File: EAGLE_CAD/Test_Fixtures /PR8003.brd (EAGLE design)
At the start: 116 x 100 mm, 43 parts, among them J1 M3_SCREW_POST

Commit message: Bumped to PR8003
New layout
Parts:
- moved JP2 53.0 mm to (78.0, 76.0), turned to 180 degrees
- moved U$24 51.6 mm to (6.00, 59.0)
- moved VOL 48.4 mm to (89.6, 5.12), turned to 180 degrees
- moved U$23 45.4 mm to (6.00, 11.0)
- moved U$20 42.2 mm to (6.00, 27.0)
- moved R2 39.5 mm to (33.0, 79.0), turned to 270 degrees
- moved U$22 37.2 mm to (6.00, 43.0)
- moved U$1 30.2 mm to (58.1, 28.4)
- moved CN1 27.9 mm to (77.0, 85.0)
- moved R16 22.6 mm to (56.9, 45.8)
- moved R13 21.7 mm to (30.8, 79.0), turned to 270 degrees
- moved R3 21.5 mm to (27.8, 79.0), turned to 270 degrees
- moved R1 21.4 mm to (25.5, 79.0), turned to 270 degrees
- moved JP1 18.9 mm to (33.0, 85.0)
- moved ISP1 16.9 mm to (65.0, 85.0), turned to 270 degrees
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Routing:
- net +5V: track 8.02 -> 188.4 mm, vias 0 -> 5
- net DEV_PRES: track 0.00 -> 138.0 mm, vias 0 -> 1
- net SPK_OUT+: track 0.00 -> 108.9 mm, vias 0 -> 1
- net SPK_OUT-: track 0.00 -> 103.7 mm, vias 0 -> 1
- net TAC2: track 0.00 -> 85.4 mm, vias 0 -> 1
- net TAC3: track 0.00 -> 81.5 mm, vias 0 -> 2
- net TAC1: track 0.00 -> 69.8 mm, vias 0 -> 1
- net ANT: track 0.00 -> 68.3 mm, vias 0 -> 1
- net N$2: track 0.00 -> 68.2 mm
- net N$3: track 0.00 -> 68.0 mm
- net N$4: track 0.00 -> 67.9 mm
- net 3.3V: track 4.76 -> 64.6 mm, vias 0 -> 2
- net COMPARATOR: track 0.00 -> 53.1 mm, vias 0 -> 2
- net A_OUT: track 0.00 -> 52.0 mm
- net REG_ENABLE: track 6.30 -> 56.6 mm
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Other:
- board size 116 x 100 mm -> 100 x 91 mm
- board text added: "PR8003"
- board text added: "SPK"
- board text removed: "1"
- board text removed: "2"
- board text removed: "ETest PR8002"
- board text removed: "EXT SPK"

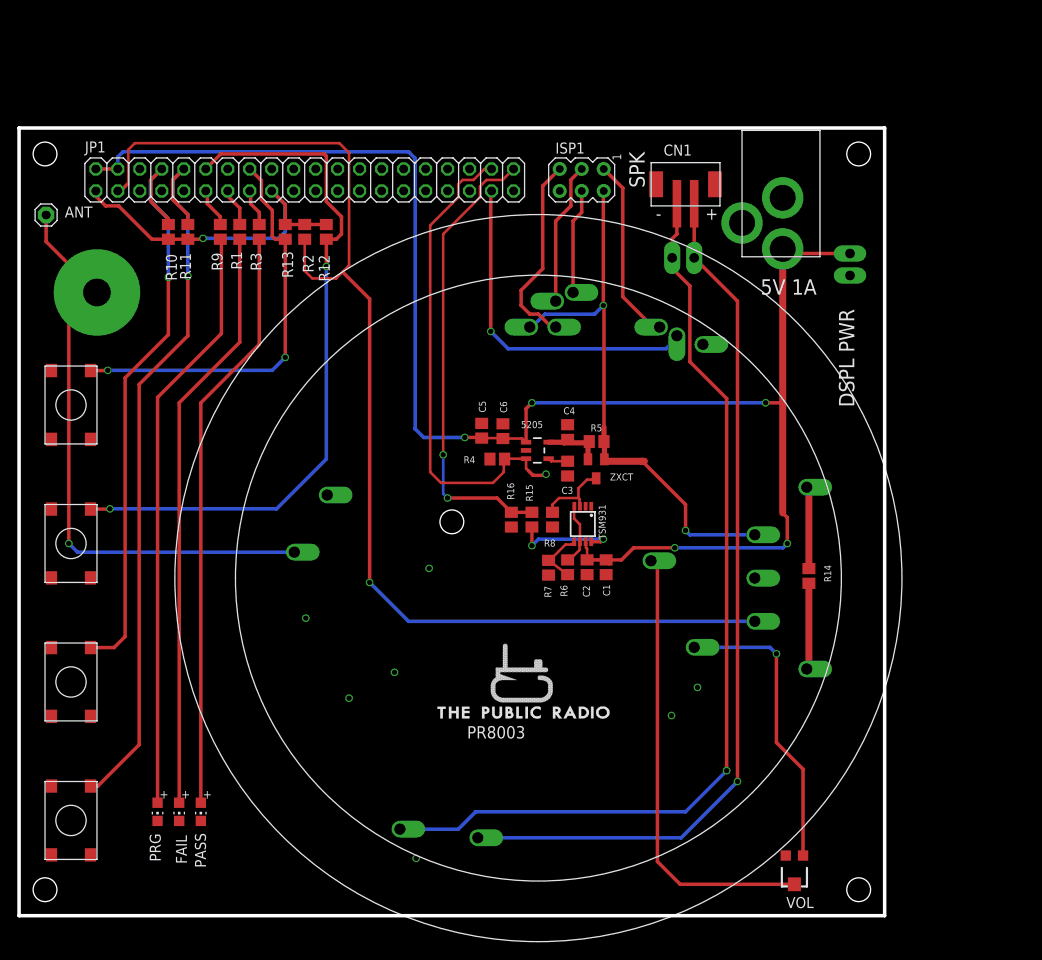
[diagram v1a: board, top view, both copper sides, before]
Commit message: PR8003 Updates
Small layout changes
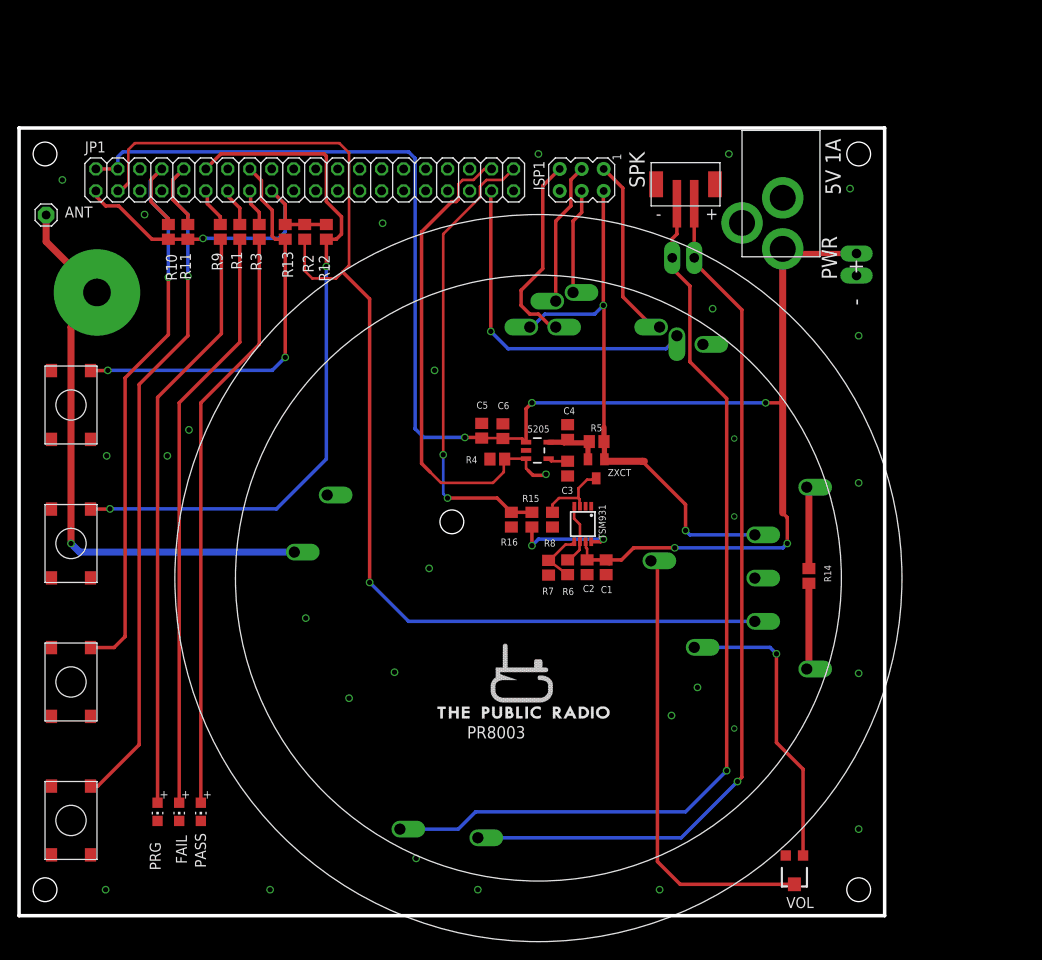
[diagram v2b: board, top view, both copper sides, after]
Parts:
- moved JP3 0.75 mm to (96.8, 76.5)
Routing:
- net REG_ENABLE: track 56.6 -> 57.7 mm
- net +5V: track 188.4 -> 189.1 mm
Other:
- board text added: "- +"
- board text added: "PWR"
- board text removed: "DSPL PWR"

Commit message: PR8003 Updates
Mostly aesthetics. Small routing changes.
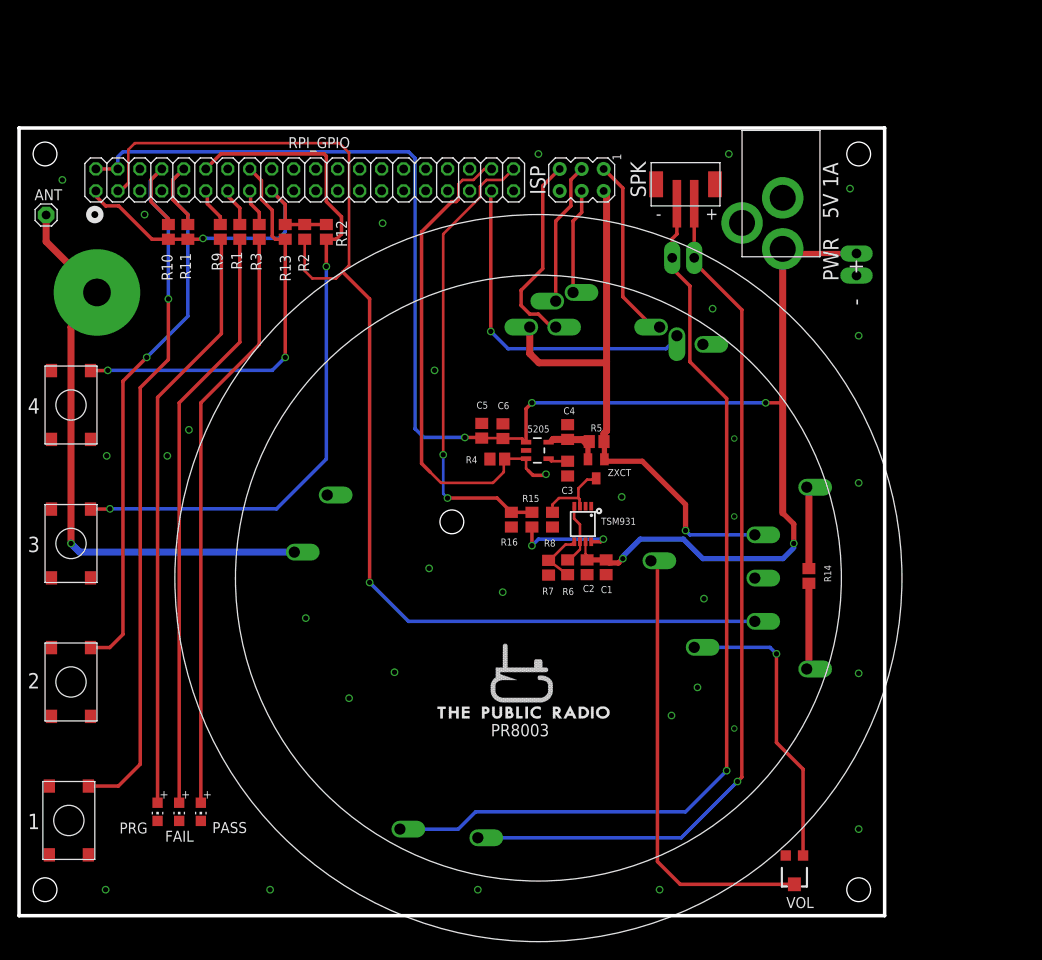
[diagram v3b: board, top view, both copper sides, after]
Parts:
- moved U$20 16.0 mm to (5.75, 11.0)
- moved U$23 16.0 mm to (6.00, 27.0)
- renumbered ISP1 to ISP, JP1 to RPI_GPIO
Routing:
- net TAC1: track 69.8 -> 86.4 mm
- net TAC2: track 85.4 -> 70.2 mm
- net 3.3V: track 64.6 -> 67.6 mm, vias 2 -> 1
- net +5V: track 189.1 -> 190.1 mm
- net N$14: track 7.89 -> 6.96 mm
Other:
- board text added: "1"
- board text added: "2"
- board text added: "3"
- board text added: "4"

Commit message: PR8003 Updates
small changes
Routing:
- net COMPARATOR: track 53.1 -> 56.1 mm
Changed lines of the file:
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@@
 <contactref element="5205" pad="4"/>
 <contactref element="C3" pad="1"/>
-<wire x1="61.4751" y1="52.85" x2="61.1751" y2="52.8" width="0.3048" layer="1"/>
-<wire x1="63.375" y1="52.5" x2="61.4751" y2="52.5" width="0.3048" layer="1"/>
+<wire x1="61.4751" y1="52.85" x2="61.1751" y2="52.8" width="0.4064" layer="1"/>
+<wire x1="63.375" y1="52.5" x2="61.4751" y2="52.5" width="0.4064" layer="1"/>
 <wire x1="61.4751" y1="52.5" x2="61.1751" y2="52.8" width="0.3048" layer="1"/>
 </signal>
@@
 <via x="60.875" y="51" extent="1-16" drill="0.6"/>
 <wire x1="58.5749" y1="52.8" x2="56.15" y2="52.8" width="0.3048" layer="1"/>
-<wire x1="58.5749" y1="52.8" x2="58.5749" y2="51.6751" width="0.3048" layer="1"/>
-<wire x1="58.5749" y1="51.6751" x2="58.8249" y2="51.4251" width="0.3048" layer="1"/>
+<wire x1="58.5749" y1="52.8" x2="58.5749" y2="51.6751" width="0.4064" layer="1"/>
+<wire x1="58.5749" y1="51.6751" x2="58.8249" y2="51.4251" width="0.4064" layer="1"/>
 <contactref element="RPI_GPIO" pad="38"/>
 <wire x1="54.59" y1="86.27" x2="53.77" y2="86.27" width="0.3048" layer="1"/>
-<wire x1="54.75" y1="50" x2="56" y2="51.25" width="0.3048" layer="1"/>
-<wire x1="56" y1="51.25" x2="56" y2="52.65" width="0.3048" layer="1"/>
+<wire x1="54.75" y1="50" x2="56" y2="51.25" width="0.4064" layer="1"/>
+<wire x1="56" y1="51.25" x2="56" y2="52.65" width="0.4064" layer="1"/>
 <wire x1="56" y1="52.65" x2="56.1" y2="52.75" width="0.3048" layer="1"/>
 <wire x1="50.75" y1="83" x2="50.75" y2="84.5" width="0.3048" layer="1"/>
@@
 <wire x1="51.25" y1="85" x2="52.5" y2="85" width="0.3048" layer="1"/>
 <wire x1="52.5" y1="85" x2="53.77" y2="86.27" width="0.3048" layer="1"/>
-<wire x1="54.75" y1="50" x2="48.75" y2="50" width="0.3048" layer="1"/>
-<wire x1="48.75" y1="50" x2="47.5" y2="51.25" width="0.3048" layer="1"/>
+<wire x1="54.75" y1="50" x2="48.75" y2="50" width="0.4064" layer="1"/>
+<wire x1="48.75" y1="50" x2="47.5" y2="51.25" width="0.4064" layer="1"/>
 <wire x1="47.5" y1="51.25" x2="46.5" y2="52.25" width="0.4064" layer="1"/>
 <wire x1="46.5" y1="52.25" x2="46.5" y2="79" width="0.4064" layer="1"/>
@@
 <contactref element="R16" pad="1"/>
 <contactref element="RPI_GPIO" pad="40"/>
-<wire x1="49.5" y1="48.25" x2="49" y2="48.75" width="0.3048" layer="16"/>
-<wire x1="49" y1="48.75" x2="49" y2="53.25" width="0.3048" layer="16"/>
 <via x="49" y="53.25" extent="1-16" drill="0.6"/>
-<wire x1="49" y1="53.25" x2="49" y2="78.75" width="0.3048" layer="1"/>
-<wire x1="49" y1="78.75" x2="53.25" y2="83" width="0.3048" layer="1"/>
+<wire x1="49" y1="53.25" x2="49" y2="78.75" width="0.4064" layer="1"/>
+<wire x1="49" y1="78.75" x2="53.25" y2="83" width="0.4064" layer="1"/>
 <wire x1="53.25" y1="83" x2="53.25" y2="84.25" width="0.3048" layer="1"/>
 <wire x1="53.25" y1="84.25" x2="54" y2="85" width="0.3048" layer="1"/>
@@
 <wire x1="55.86" y1="85" x2="57.13" y2="86.27" width="0.3048" layer="1"/>
 <wire x1="59.25" y1="46.6" x2="56.875" y2="46.6" width="0.4064" layer="1"/>
-<via x="49.5" y="48.25" extent="1-16" drill="0.6"/>
 <wire x1="56.875" y1="46.6" x2="55.225" y2="48.25" width="0.4064" layer="1"/>
-<wire x1="55.225" y1="48.25" x2="49.5" y2="48.25" width="0.4064" layer="1"/>
+<wire x1="55.225" y1="48.25" x2="47.4375" y2="48.25" width="0.4064" layer="1"/>
+<wire x1="47.4375" y1="48.25" x2="46.875" y2="48.8125" width="0.4064" layer="1"/>
+<via x="46.875" y="48.8125" extent="1-16" drill="0.6"/>
+<wire x1="46.875" y1="48.8125" x2="46.875" y2="50.8125" width="0.4064" layer="16"/>
+<wire x1="46.875" y1="50.8125" x2="48.375" y2="52.3125" width="0.4064" layer="16"/>
+<wire x1="48.375" y1="52.3125" x2="48.4375" y2="52.3125" width="0.4064" layer="16"/>
+<wire x1="48.4375" y1="52.3125" x2="48.875" y2="52.75" width="0.4064" layer="16"/>
+<wire x1="48.875" y1="52.75" x2="48.875" y2="53.125" width="0.4064" layer="16"/>
+<wire x1="48.875" y1="53.125" x2="49" y2="53.25" width="0.4064" layer="16"/>
 </signal>
 <signal name="+3V3">
@@
 <contactref element="C6" pad="1"/>
 <wire x1="65.625" y1="41.1" x2="67.825" y2="41.1" width="0.6096" layer="1"/>
-<wire x1="53.45" y1="55.175" x2="55.85" y2="55.175" width="0.3048" layer="1"/>
+<wire x1="53.45" y1="55.175" x2="55.85" y2="55.175" width="0.4064" layer="1"/>
 <wire x1="55.85" y1="55.175" x2="55.9" y2="55.125" width="0.3048" layer="1"/>
-<wire x1="55.9" y1="55.125" x2="58.1499" y2="55.125" width="0.3048" layer="1"/>
+<wire x1="55.9" y1="55.125" x2="58.1499" y2="55.125" width="0.4064" layer="1"/>
 <wire x1="58.1499" y1="55.125" x2="58.5749" y2="54.7" width="0.3048" layer="1"/>
 <contactref element="JP3" pad="1"/>

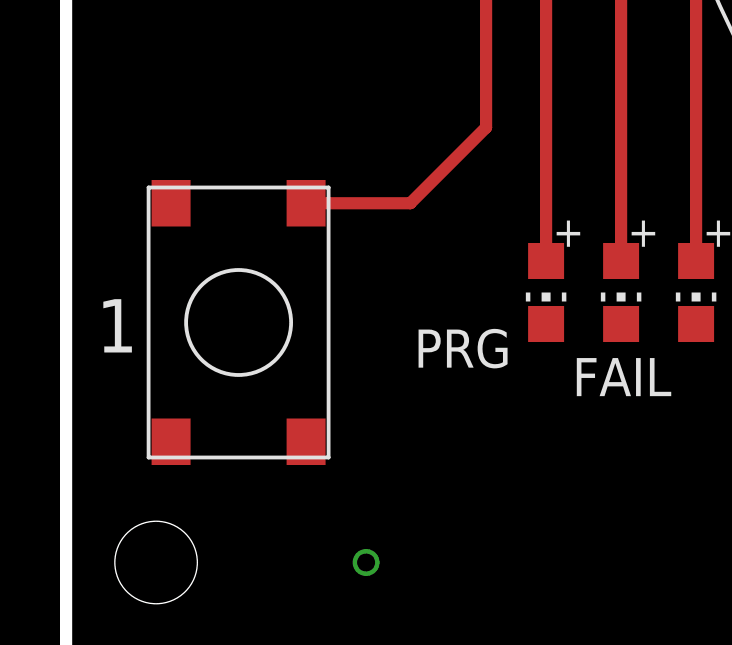
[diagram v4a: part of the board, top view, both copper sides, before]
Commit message: PR8003
Bottom button move
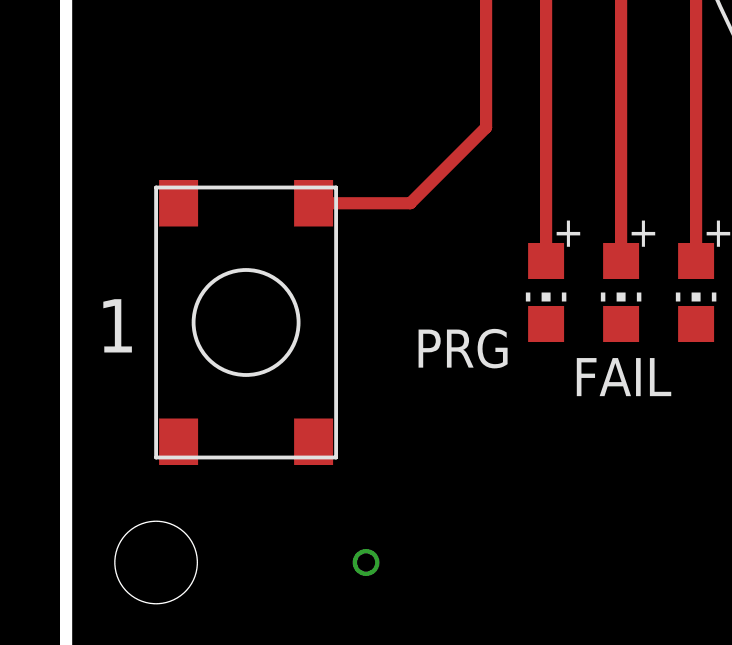
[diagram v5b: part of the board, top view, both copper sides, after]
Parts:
- moved U$20 0.25 mm to (6.00, 11.0)
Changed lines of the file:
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@@
 <attribute name="NAME" x="60.8145" y="83.298" size="1.778" layer="25" font="vector" ratio="16" rot="R90"/>
 </element>
-<element name="U$20" library="PR_Parts_Library" package="C&amp;K_PTS645_SMT" value="C&amp;K_PTS645" x="5.75" y="11" rot="R90">
-<attribute name="MFG_PN" value="PTS645SM43SMTR92 LFS" x="5.75" y="11" size="1.778" layer="27" rot="R90" display="off"/>
+<element name="U$20" library="PR_Parts_Library" package="C&amp;K_PTS645_SMT" value="C&amp;K_PTS645" x="6" y="11" rot="R90">
+<attribute name="MFG_PN" value="PTS645SM43SMTR92 LFS" x="6" y="11" size="1.778" layer="27" rot="R90" display="off"/>
 </element>
 <element name="U$22" library="PR_Parts_Library" package="C&amp;K_PTS645_SMT" value="C&amp;K_PTS645" x="6" y="43" rot="R90">
@@
 <wire x1="15.125" y1="82.625" x2="15.125" y2="84.905" width="0.3048" layer="16"/>
 <wire x1="15.125" y1="84.905" x2="15.375" y2="85.155" width="0.3048" layer="16"/>
-<wire x1="8" y1="14.975" x2="11.475" y2="14.975" width="0.4064" layer="1"/>
+<wire x1="8.25" y1="14.975" x2="11.475" y2="14.975" width="0.4064" layer="1"/>
 <wire x1="11.475" y1="14.975" x2="14" y2="17.5" width="0.4064" layer="1"/>
 <wire x1="14" y1="17.5" x2="14" y2="61" width="0.4064" layer="1"/>
